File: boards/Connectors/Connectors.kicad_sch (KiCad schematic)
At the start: 17 parts, among them J1 DIN-5, J2 DIN-5, J3 DIN-5, SW1 RotaryEncoder_Switch, SW2 RotaryEncoder_Switch, SW3 RotaryEncoder_Switch, SW4 RotaryEncoder_Switch

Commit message: Fixed MIDI interfaces
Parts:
- removed Ctrl1: Ctrl-1, symbol Connector_Generic:Conn_01x04
- removed Ctrl2: Ctrl-2, symbol Connector_Generic:Conn_01x04
- removed Ctrl3: Ctrl-3, symbol Connector_Generic:Conn_01x04
- removed Ctrl4: Ctrl-4, symbol Connector_Generic:Conn_01x04
- removed J1, J2, J3: DIN-5, symbol Connector:DIN-5
- removed MIDI_IN, MIDI_OUT, MIDI_THRU: Conn_01x05, symbol Connector_Generic:Conn_01x05
- added J1, J2, J3: DIN-5_180degree, symbol Connector:DIN-5_180degree
- added J4: Ctrl-3, Connector_PinHeader_2.54mm:PinHeader_2x02_P2.54mm_Horizontal, symbol Connector_Generic:Conn_02x02_Odd_Even
- added J5: Ctrl-4, Connector_PinHeader_2.54mm:PinHeader_2x02_P2.54mm_Horizontal, symbol Connector_Generic:Conn_02x02_Odd_Even
- added J6: Ctrl-1, Connector_PinHeader_2.54mm:PinHeader_2x02_P2.54mm_Horizontal, symbol Connector_Generic:Conn_02x02_Odd_Even
- added J7: Ctrl-2, Connector_PinHeader_2.54mm:PinHeader_2x02_P2.54mm_Horizontal, symbol Connector_Generic:Conn_02x02_Odd_Even
- added J8: Btn-1, Connector_PinHeader_2.54mm:PinHeader_2x02_P2.54mm_Horizontal, symbol Connector_Generic:Conn_02x02_Odd_Even
- added J9: Btn-2, Connector_PinHeader_2.54mm:PinHeader_2x02_P2.54mm_Horizontal, symbol Connector_Generic:Conn_02x02_Odd_Even
- added MIDI1: MIDI_IN, Connector_PinHeader_2.54mm:PinHeader_2x03_P2.54mm_Horizontal, symbol Connector_Generic:Conn_02x03_Odd_Even
- added MIDI2: MIDI_THRU, Connector_PinHeader_2.54mm:PinHeader_2x03_P2.54mm_Horizontal, symbol Connector_Generic:Conn_02x03_Odd_Even
- added MIDI3: MIDI_OUT, Connector_PinHeader_2.54mm:PinHeader_2x03_P2.54mm_Horizontal, symbol Connector_Generic:Conn_02x03_Odd_Even
- added SW5, SW6, SW7, SW8: SW_DIP_x01, symbol Switch:SW_DIP_x01
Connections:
- net at SW3.C, SW3.S1: now also J6.4 (Pin_4)
- net at SW3.B: now also J6.1 (Pin_1)
- net at SW3.A: now also J6.3 (Pin_3)
- net at SW3.S2: now also J6.2 (Pin_2)
- net at D1.1 (K): now also MIDI1.6 (Pin_6)
- net at D1.2 (A): now also MIDI1.5 (Pin_5)
- net at SW2.A: now also J5.3 (Pin_3)
- net at SW2.B: now also J5.1 (Pin_1)
- net at SW2.C, SW2.S1: now also J5.4 (Pin_4)
- net at SW2.S2: now also J5.2 (Pin_2)
- net at SW1.A: now also J4.3 (Pin_3)
- net at SW1.B: now also J4.1 (Pin_1)
- net at SW1.C, SW1.S1: now also J4.4 (Pin_4)
- net at SW1.S2: now also J4.2 (Pin_2)
- net at SW4.C, SW4.S1: now also J7.4 (Pin_4)
- net at SW4.B: now also J7.1 (Pin_1)
- net at SW4.A: now also J7.3 (Pin_3)
- net at SW4.S2: now also J7.2 (Pin_2)
- net at D2.1 (K): now also MIDI2.6 (Pin_6)
- net at D2.2 (A): now also MIDI2.5 (Pin_5)
- net at D3.2 (A): now also MIDI3.5 (Pin_5)
- net at D3.1 (K): now also MIDI3.6 (Pin_6)
- new net: J8.1 (Pin_1), SW5.1
- new net: J8.2 (Pin_2), SW5.2
- new net: J8.3 (Pin_3), SW8.1
- new net: J8.4 (Pin_4), SW8.2
- new net: J1.4, MIDI1.1 (Pin_1)
- new net: J1.2, MIDI1.2 (Pin_2)
- new net: J1.5, MIDI1.3 (Pin_3)
- new net: J2.2, MIDI2.2 (Pin_2)
- new net: J2.4, MIDI2.1 (Pin_1)
- new net: J2.5, MIDI2.3 (Pin_3)
- new net: J9.1 (Pin_1), SW7.1
- new net: J9.2 (Pin_2), SW7.2
- new net: J9.3 (Pin_3), SW6.1
- new net: J9.4 (Pin_4), SW6.2
- new net: J3.2, MIDI3.2 (Pin_2)
- new net: J3.4, MIDI3.1 (Pin_1)
- new net: J3.5, MIDI3.3 (Pin_3)

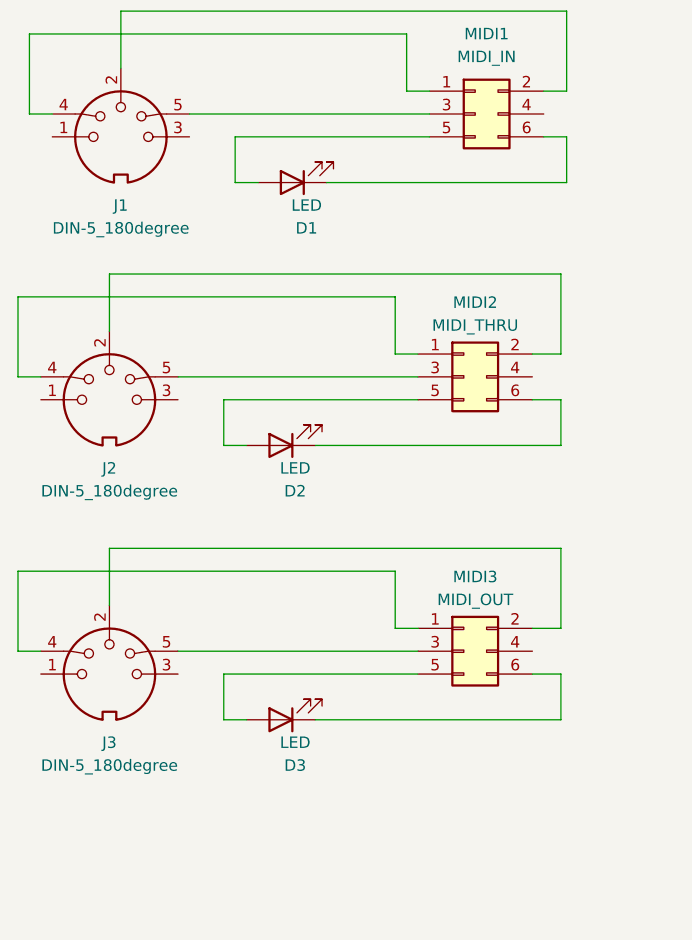
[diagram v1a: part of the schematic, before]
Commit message: Using 74LS07 OC buffer to avoid excessive LED currents
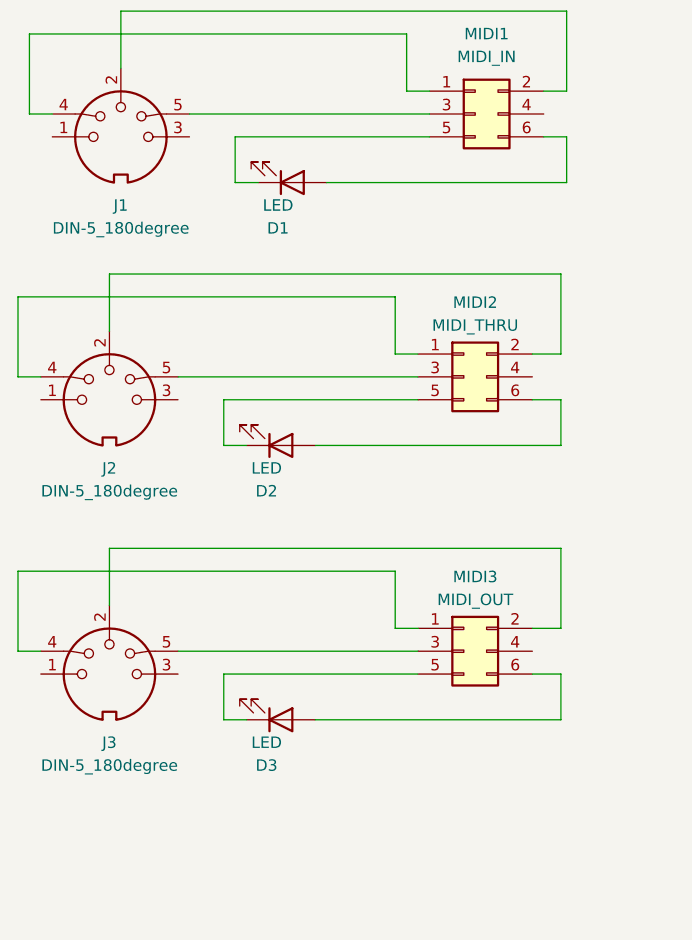
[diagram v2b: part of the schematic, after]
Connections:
- net at MIDI1.5 (Pin_5): now also D1.1 (K); no longer D1.2 (A)
- net at MIDI1.6 (Pin_6): now also D1.2 (A); no longer D1.1 (K)
- net at D2.1 (K): now also MIDI2.5 (Pin_5); no longer MIDI2.6 (Pin_6)
- net at D2.2 (A): now also MIDI2.6 (Pin_6); no longer MIDI2.5 (Pin_5)
- net at D3.1 (K): now also MIDI3.5 (Pin_5); no longer MIDI3.6 (Pin_6)
- net at D3.2 (A): now also MIDI3.6 (Pin_6); no longer MIDI3.5 (Pin_5)
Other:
- moved on the sheet: D1, D2, D3

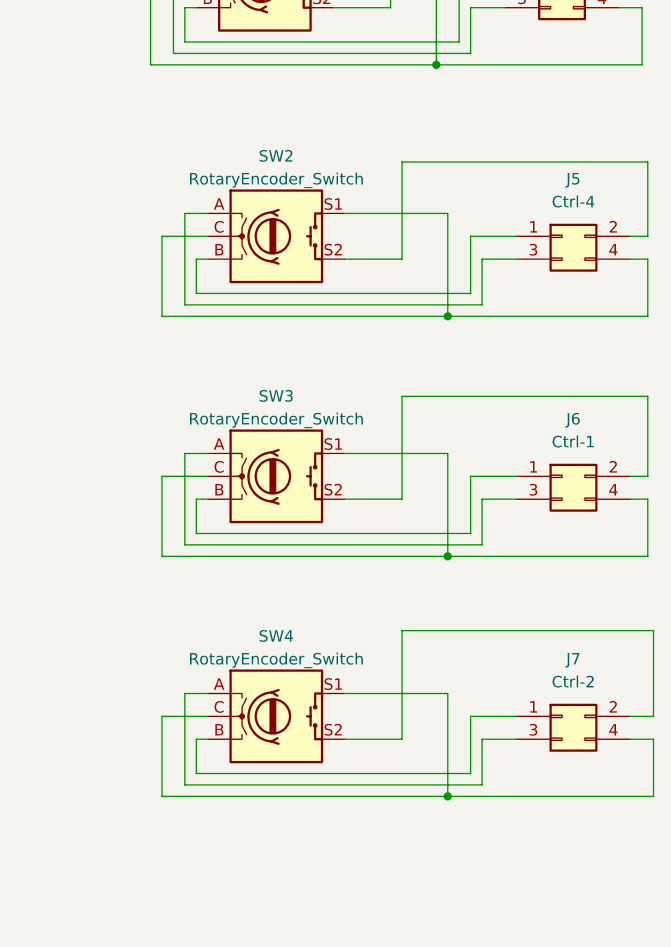
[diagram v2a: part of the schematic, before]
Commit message: Fixed rotary switches connections
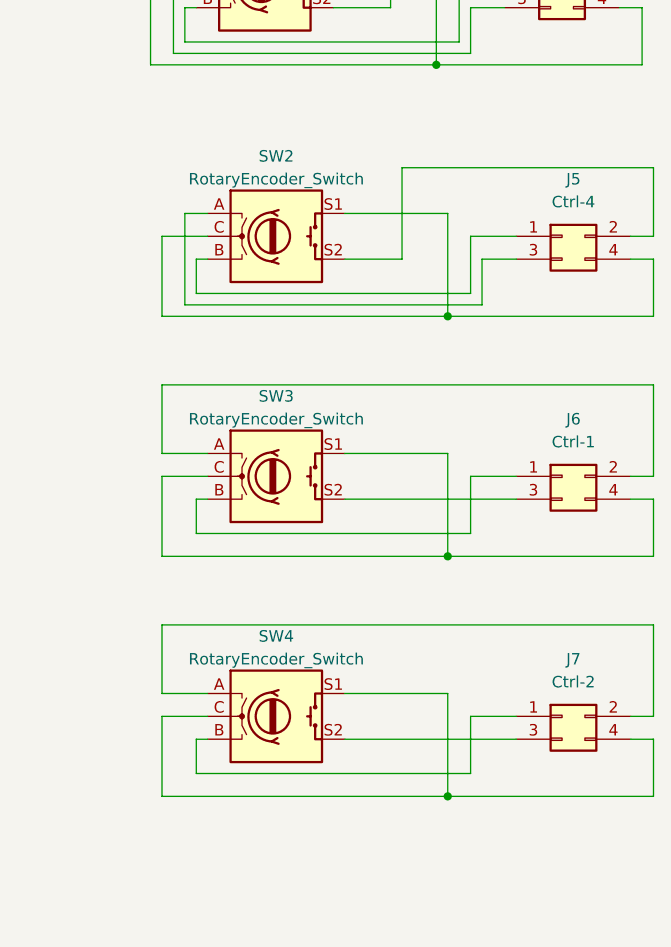
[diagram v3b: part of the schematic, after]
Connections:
- net at J7.2 (Pin_2): now also SW4.A; no longer SW4.S2
- net at J7.3 (Pin_3): now also SW4.S2; no longer SW4.A
- net at J6.2 (Pin_2): now also SW3.A; no longer SW3.S2
- net at J6.3 (Pin_3): now also SW3.S2; no longer SW3.A
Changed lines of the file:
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@@
 	(wire
 		(pts
-			(xy 171.45 123.19) (xy 165.1 123.19)
+			(xy 165.1 123.19) (xy 184.15 123.19)
 		)
 		(stroke
@@
 	(wire
 		(pts
-			(xy 171.45 69.85) (xy 171.45 59.055)
+			(xy 171.45 69.85) (xy 171.45 59.69)
 		)
 		(stroke
@@
 	(wire
 		(pts
-			(xy 198.755 69.85) (xy 198.755 76.2)
+			(xy 199.39 69.85) (xy 199.39 76.2)
 		)
 		(stroke
@@
 	(wire
 		(pts
-			(xy 147.32 128.27) (xy 180.34 128.27)
-		)
-		(stroke
-			(width 0)
-			(type default)
-		)
-	)
-	(wire
-		(pts
 			(xy 50.8 158.115) (xy 45.72 158.115)
 		)
@@
 	(wire
 		(pts
-			(xy 196.85 69.85) (xy 198.755 69.85)
+			(xy 196.85 69.85) (xy 199.39 69.85)
 		)
 		(stroke
@@
 	(wire
 		(pts
-			(xy 147.32 101.6) (xy 180.34 101.6)
-		)
-		(stroke
-			(width 0)
-			(type default)
-		)
-	)
-	(wire
-		(pts
 			(xy 119.38 157.48) (xy 119.38 170.815)
 		)
@@
 	(wire
 		(pts
-			(xy 180.34 101.6) (xy 180.34 96.52)
-		)
-		(stroke
-			(width 0)
-			(type default)
-		)
-	)
-	(wire
-		(pts
 			(xy 144.78 76.2) (xy 176.53 76.2)
 		)
@@
 	(wire
 		(pts
-			(xy 171.45 96.52) (xy 171.45 85.09)
-		)
-		(stroke
-			(width 0)
-			(type default)
-		)
-	)
-	(wire
-		(pts
 			(xy 80.01 92.71) (xy 38.1 92.71)
 		)
@@
 	(wire
 		(pts
-			(xy 199.39 111.125) (xy 199.39 120.65)
+			(xy 199.39 110.49) (xy 199.39 120.65)
 		)
 		(stroke
@@
 	(wire
 		(pts
-			(xy 147.32 118.11) (xy 147.32 128.27)
-		)
-		(stroke
-			(width 0)
-			(type default)
-		)
-	)
-	(wire
-		(pts
 			(xy 144.78 120.65) (xy 144.78 129.54)
 		)
@@
 	(wire
 		(pts
+			(xy 199.39 83.82) (xy 199.39 93.98)
+		)
+		(stroke
+			(width 0)
+			(type default)
+		)
+	)
+	(wire
+		(pts
 			(xy 69.215 158.115) (xy 63.5 158.115)
 		)
@@
 	(wire
 		(pts
-			(xy 147.32 91.44) (xy 147.32 101.6)
+			(xy 144.78 91.44) (xy 144.78 83.82)
 		)
 		(stroke
@@
 	(wire
 		(pts
-			(xy 180.34 123.19) (xy 184.15 123.19)
-		)
-		(stroke
-			(width 0)
-			(type default)
-		)
-	)
-	(wire
-		(pts
 			(xy 179.07 120.65) (xy 184.15 120.65)
 		)
@@
 	(wire
 		(pts
-			(xy 198.755 102.87) (xy 176.53 102.87)
+			(xy 199.39 102.87) (xy 176.53 102.87)
+		)
+		(stroke
+			(width 0)
+			(type default)
+		)
+	)
+	(wire
+		(pts
+			(xy 144.78 118.11) (xy 149.86 118.11)
 		)
 		(stroke
@@
 	(wire
 		(pts
-			(xy 198.755 85.09) (xy 198.755 93.98)
-		)
-		(stroke
-			(width 0)
-			(type default)
-		)
-	)
-	(wire
-		(pts
 			(xy 147.32 41.91) (xy 147.32 45.72)
 		)
@@
 	(wire
 		(pts
-			(xy 198.755 96.52) (xy 198.755 102.87)
-		)
-		(stroke
-			(width 0)
-			(type default)
-		)
-	)
-	(wire
-		(pts
-			(xy 149.86 91.44) (xy 147.32 91.44)
+			(xy 199.39 96.52) (xy 199.39 102.87)
 		)
 		(stroke
@@
 	(wire
 		(pts
+			(xy 144.78 118.11) (xy 144.78 110.49)
+		)
+		(stroke
+			(width 0)
+			(type default)
+		)
+	)
+	(wire
+		(pts
 			(xy 45.085 155.575) (xy 50.8 155.575)
 		)
@@
 	(wire
 		(pts
-			(xy 198.755 59.055) (xy 198.755 67.31)
+			(xy 199.39 59.69) (xy 199.39 67.31)
 		)
 		(stroke
@@
 	(wire
 		(pts
+			(xy 144.78 91.44) (xy 149.86 91.44)
+		)
+		(stroke
+			(width 0)
+			(type default)
+		)
+	)
+	(wire
+		(pts
 			(xy 57.15 41.91) (xy 83.82 41.91)
 		)
@@
 	(wire
 		(pts
-			(xy 171.45 96.52) (xy 165.1 96.52)
+			(xy 165.1 96.52) (xy 184.15 96.52)
 		)
 		(stroke
@@
 	(wire
 		(pts
-			(xy 171.45 123.19) (xy 171.45 111.125)
-		)
-		(stroke
-			(width 0)
-			(type default)
-		)
-	)
-	(wire
-		(pts
 			(xy 179.07 127) (xy 179.07 120.65)
 		)
@@
 	(wire
 		(pts
-			(xy 149.86 118.11) (xy 147.32 118.11)
-		)
-		(stroke
-			(width 0)
-			(type default)
-		)
-	)
-	(wire
-		(pts
 			(xy 149.86 67.31) (xy 144.78 67.31)
 		)
@@
 	(wire
 		(pts
-			(xy 171.45 59.055) (xy 198.755 59.055)
-		)
-		(stroke
-			(width 0)
-			(type default)
-		)
-	)
-	(wire
-		(pts
-			(xy 198.755 67.31) (xy 196.85 67.31)
+			(xy 171.45 59.69) (xy 199.39 59.69)
+		)
+		(stroke
+			(width 0)
+			(type default)
+		)
+	)
+	(wire
+		(pts
+			(xy 199.39 67.31) (xy 196.85 67.31)
 		)
 		(stroke
@@
 	(wire
 		(pts
+			(xy 144.78 110.49) (xy 199.39 110.49)
+		)
+		(stroke
+			(width 0)
+			(type default)
+		)
+	)
+	(wire
+		(pts
 			(xy 163.83 36.83) (xy 175.26 36.83)
 		)
@@
 	(wire
 		(pts
-			(xy 171.45 111.125) (xy 199.39 111.125)
-		)
-		(stroke
-			(width 0)
-			(type default)
-		)
-	)
-	(wire
-		(pts
 			(xy 69.215 155.575) (xy 69.215 143.51)
 		)
@@
 	(wire
 		(pts
-			(xy 196.85 96.52) (xy 198.755 96.52)
+			(xy 196.85 96.52) (xy 199.39 96.52)
 		)
 		(stroke
@@
 	(wire
 		(pts
-			(xy 180.34 96.52) (xy 184.15 96.52)
-		)
-		(stroke
-			(width 0)
-			(type default)
-		)
-	)
-	(wire
-		(pts
-			(xy 198.755 93.98) (xy 196.85 93.98)
-		)
-		(stroke
-			(width 0)
-			(type default)
-		)
-	)
-	(wire
-		(pts
-			(xy 198.755 76.2) (xy 176.53 76.2)
-		)
-		(stroke
-			(width 0)
-			(type default)
-		)
-	)
-	(wire
-		(pts
-			(xy 171.45 85.09) (xy 198.755 85.09)
+			(xy 144.78 83.82) (xy 199.39 83.82)
+		)
+		(stroke
+			(width 0)
+			(type default)
+		)
+	)
+	(wire
+		(pts
+			(xy 199.39 93.98) (xy 196.85 93.98)
+		)
+		(stroke
+			(width 0)
+			(type default)
+		)
+	)
+	(wire
+		(pts
+			(xy 199.39 76.2) (xy 176.53 76.2)
 		)
 		(stroke
@@
 		)
 		(stroke
-			(width 0)
-			(type default)
-		)
-	)
-	(wire
-		(pts
-			(xy 180.34 128.27) (xy 180.34 123.19)
-		)
-		(stroke
